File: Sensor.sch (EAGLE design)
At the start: 16 parts

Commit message: Changed board dimensions
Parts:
- removed H2: MOUNT-HOLE-NPTH-M4, FormE:MOUNT-HOLE-NPTH-M4
- added H3, H4: MOUNT-HOLE3.0, holes:MOUNT-HOLE3.0
- H1: value MOUNT-HOLE-NPTH-M4 -> MOUNT-HOLE3.0; device FormE:MOUNT-HOLE-NPTH-M4 -> holes:MOUNT-HOLE3.0
- R1: value (none) -> 2M
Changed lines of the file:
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@@
 </classes>
 <parts>
-<part name="R1" library="pot" library_urn="urn:adsk.eagle:library:331" deviceset="TRIM_US-" device="CT6" package3d_urn="urn:adsk.eagle:package:22692/1"/>
+<part name="R1" library="pot" library_urn="urn:adsk.eagle:library:331" deviceset="TRIM_US-" device="CT6" package3d_urn="urn:adsk.eagle:package:22692/1" value="2M"/>
 <part name="U$1" library="FormE" deviceset="TLV9102" device=""/>
 <part name="C1" library="rcl" library_urn="urn:adsk.eagle:library:334" deviceset="C-US" device="C1206" package3d_urn="urn:adsk.eagle:package:23618/2"/>
@@
 <part name="U$2" library="FormE" deviceset="709155001610004" device=""/>
 <part name="U$3" library="FormE" deviceset="709155001610004" device=""/>
-<part name="H1" library="FormE" deviceset="MOUNT-HOLE-NPTH" device="-M4"/>
-<part name="H2" library="FormE" deviceset="MOUNT-HOLE-NPTH" device="-M4"/>
 <part name="TP7" library="SparkFun-Connectors" library_urn="urn:adsk.eagle:library:513" deviceset="TEST-POINT" device="3X5" package3d_urn="urn:adsk.eagle:package:38285/1"/>
+<part name="H3" library="holes" library_urn="urn:adsk.eagle:library:237" deviceset="MOUNT-HOLE" device="3.0" package3d_urn="urn:adsk.eagle:package:14277/1"/>
+<part name="H4" library="holes" library_urn="urn:adsk.eagle:library:237" deviceset="MOUNT-HOLE" device="3.0" package3d_urn="urn:adsk.eagle:package:14277/1"/>
+<part name="H1" library="holes" library_urn="urn:adsk.eagle:library:237" deviceset="MOUNT-HOLE" device="3.0" package3d_urn="urn:adsk.eagle:package:14277/1"/>
 </parts>
 <sheets>
@@
 <instance part="U$2" gate="G$1" x="50.8" y="86.36" smashed="yes"/>
 <instance part="U$3" gate="G$1" x="50.8" y="76.2" smashed="yes"/>
-<instance part="H1" gate="G$1" x="71.12" y="35.56" smashed="yes"/>
-<instance part="H2" gate="G$1" x="91.44" y="35.56" smashed="yes"/>
 <instance part="TP7" gate="G$1" x="99.06" y="58.42" smashed="yes">
 <attribute name="NAME" x="104.14" y="58.42" size="1.778" layer="95" font="vector"/>
+</instance>
+<instance part="H3" gate="G$1" x="71.12" y="45.72" smashed="yes">
+<attribute name="NAME" x="73.152" y="46.3042" size="1.778" layer="95"/>
+<attribute name="VALUE" x="73.152" y="43.2562" size="1.778" layer="96"/>
+</instance>
+<instance part="H4" gate="G$1" x="71.12" y="38.1" smashed="yes">
+<attribute name="NAME" x="73.152" y="38.6842" size="1.778" layer="95"/>
+<attribute name="VALUE" x="73.152" y="35.6362" size="1.778" layer="96"/>
+</instance>
+<instance part="H1" gate="G$1" x="71.12" y="30.48" smashed="yes">
+<attribute name="NAME" x="73.152" y="31.0642" size="1.778" layer="95"/>
+<attribute name="VALUE" x="73.152" y="28.0162" size="1.778" layer="96"/>
 </instance>
 </instances>
@@
 <pinref part="TP7" gate="G$1" pin="1"/>
 <junction x="99.06" y="58.42"/>
-<pinref part="TP7" gate="G$1" pin="1"/>
 </segment>
 <segment>

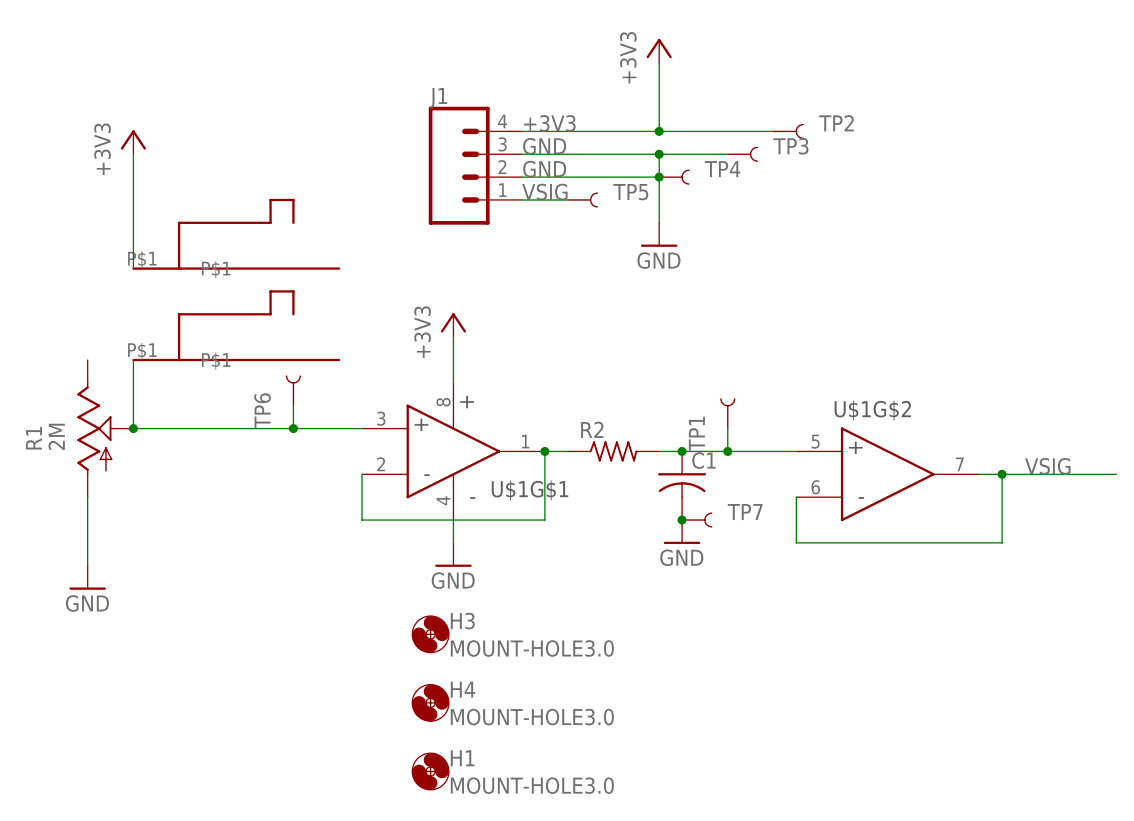
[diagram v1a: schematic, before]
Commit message: Added cart from digikey, updated schematic with values
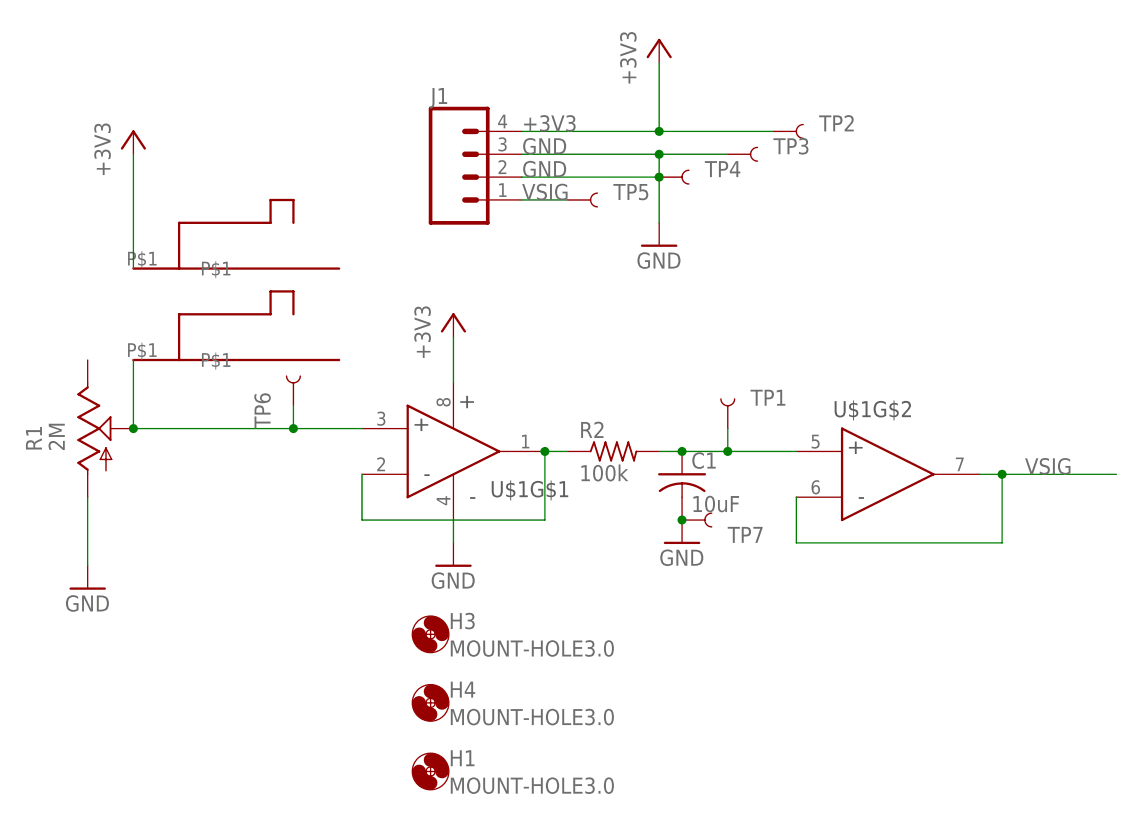
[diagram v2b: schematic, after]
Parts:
- C1: value (none) -> 10uF
- R2: value (none) -> 100k
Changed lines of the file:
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@@
 <part name="R1" library="pot" library_urn="urn:adsk.eagle:library:331" deviceset="TRIM_US-" device="CT6" package3d_urn="urn:adsk.eagle:package:22692/1" value="2M"/>
 <part name="U$1" library="FormE" deviceset="TLV9102" device=""/>
-<part name="C1" library="rcl" library_urn="urn:adsk.eagle:library:334" deviceset="C-US" device="C1206" package3d_urn="urn:adsk.eagle:package:23618/2"/>
-<part name="R2" library="rcl" library_urn="urn:adsk.eagle:library:334" deviceset="R-US_" device="R1206" package3d_urn="urn:adsk.eagle:package:23540/2"/>
+<part name="C1" library="rcl" library_urn="urn:adsk.eagle:library:334" deviceset="C-US" device="C1206" package3d_urn="urn:adsk.eagle:package:23618/2" value="10uF"/>
+<part name="R2" library="rcl" library_urn="urn:adsk.eagle:library:334" deviceset="R-US_" device="R1206" package3d_urn="urn:adsk.eagle:package:23540/2" value="100k"/>
 <part name="J1" library="SparkFun-Connectors" library_urn="urn:adsk.eagle:library:513" deviceset="CONN_04" device="SCREW" package3d_urn="urn:adsk.eagle:package:38090/1"/>
 <part name="GND1" library="supply1" library_urn="urn:adsk.eagle:library:371" deviceset="GND" device=""/>
@@
 </instance>
 <instance part="TP1" gate="G$1" x="104.14" y="68.58" smashed="yes" rot="R90">
-<attribute name="NAME" x="101.6" y="66.04" size="1.778" layer="95" font="vector" rot="R90"/>
+<attribute name="NAME" x="106.68" y="71.12" size="1.778" layer="95" font="vector"/>
 </instance>
 <instance part="TP2" gate="G$1" x="109.22" y="101.6" smashed="yes">
@@
 <instance part="U$3" gate="G$1" x="50.8" y="76.2" smashed="yes"/>
 <instance part="TP7" gate="G$1" x="99.06" y="58.42" smashed="yes">
-<attribute name="NAME" x="104.14" y="58.42" size="1.778" layer="95" font="vector"/>
+<attribute name="NAME" x="104.14" y="55.88" size="1.778" layer="95" font="vector"/>
 </instance>
 <instance part="H3" gate="G$1" x="71.12" y="45.72" smashed="yes">
